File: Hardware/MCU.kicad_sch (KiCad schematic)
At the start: 40 parts, among them SW301 RESET, U301 STM32F722ZETx, Y301 24MHz

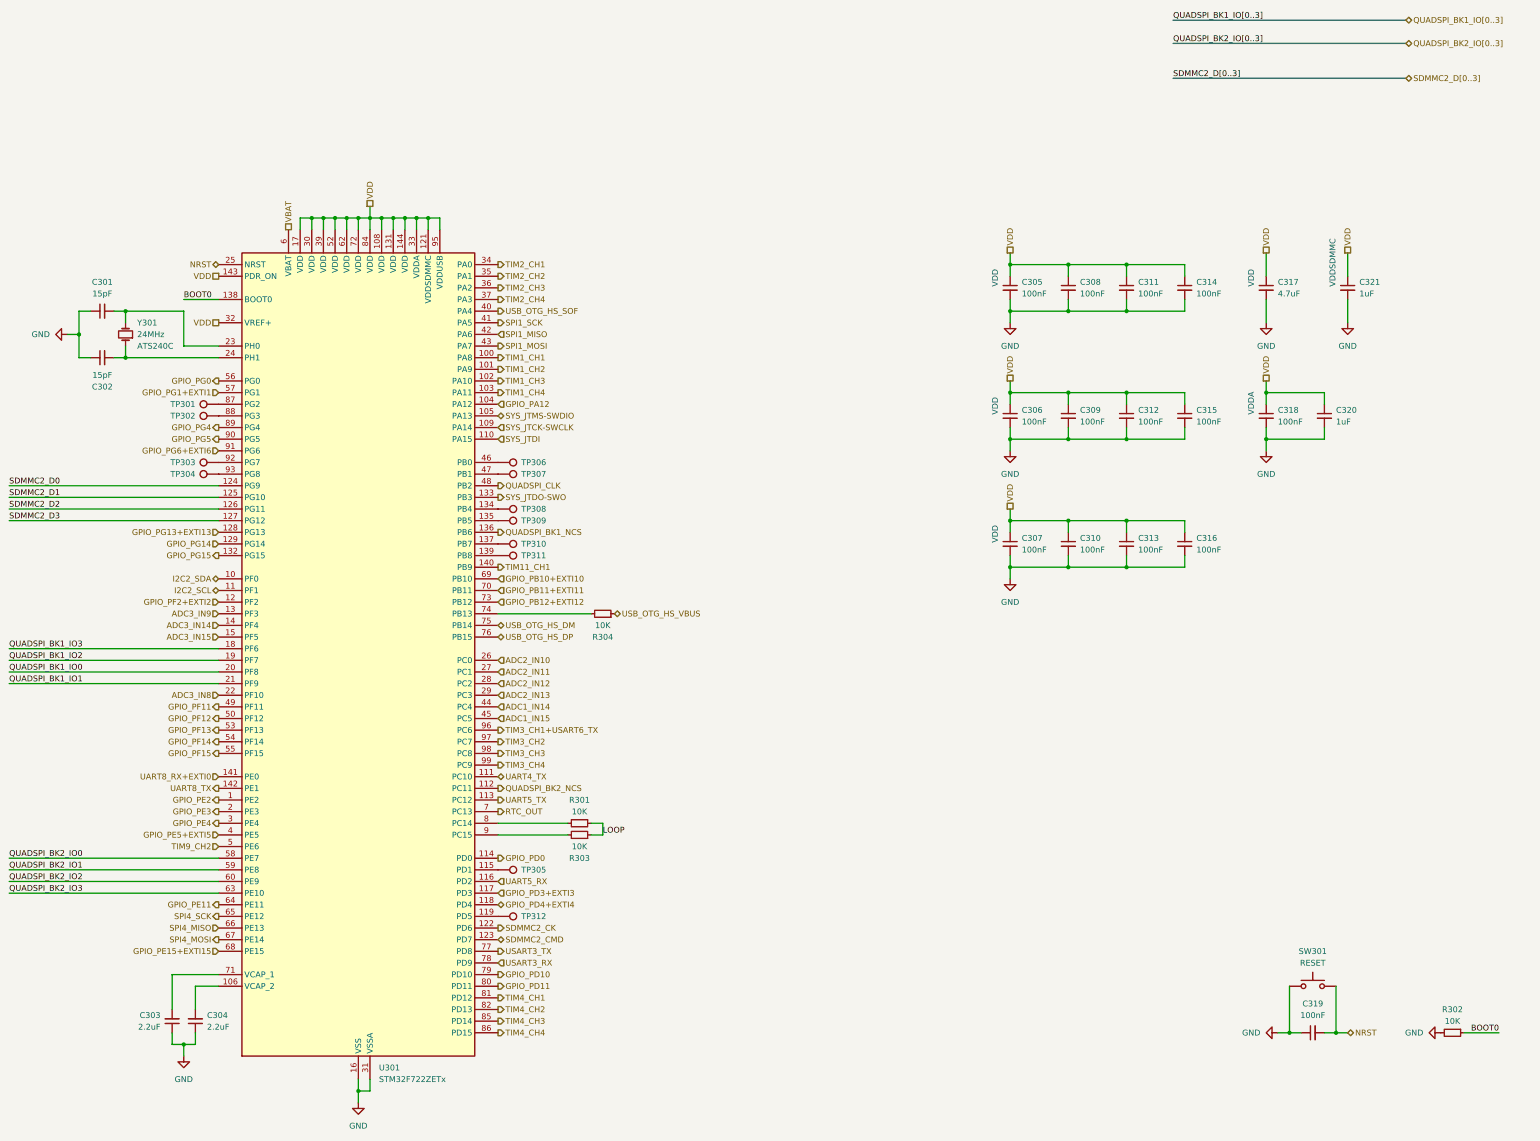
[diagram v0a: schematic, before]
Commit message: Schematic layout fixes
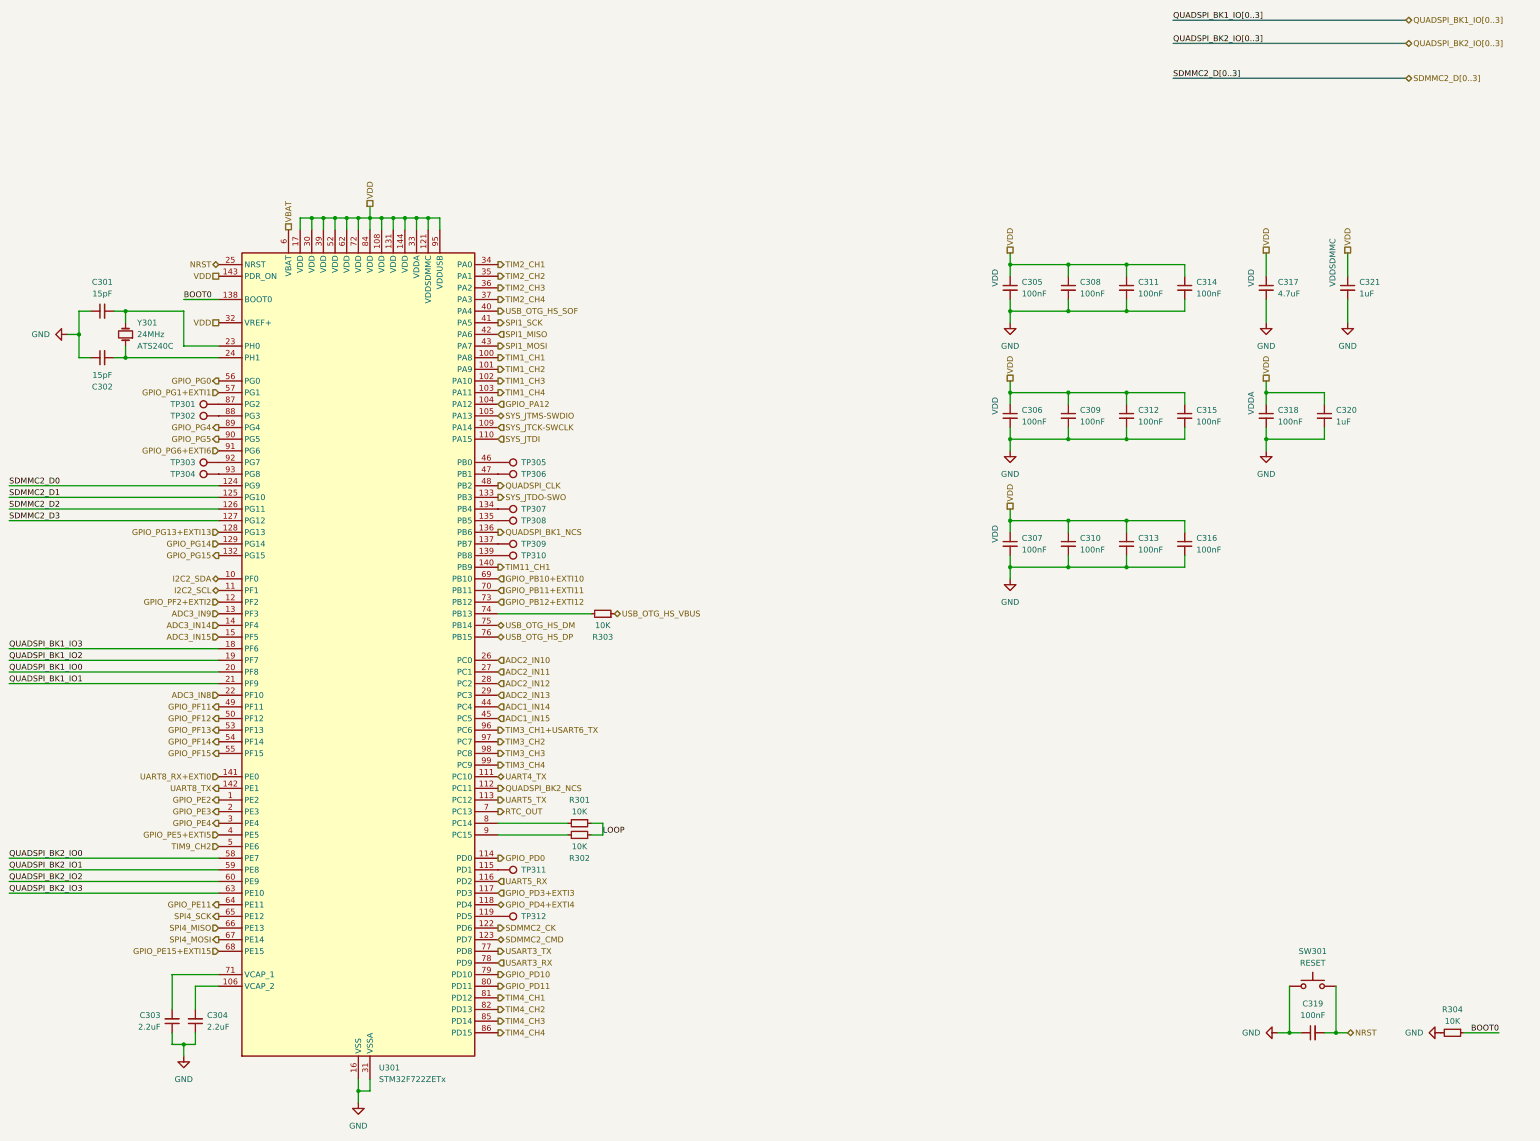
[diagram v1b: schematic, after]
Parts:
- renumbered R303 to R302, R304 to R303, R302 to R304, TP306 to TP305, TP307 to TP306, TP308 to TP307, TP309 to TP308, TP310 to TP309, TP311 to TP310, TP305 to TP311
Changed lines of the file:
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@@
   (symbol (lib_id "Connector:TestPoint") (at 182.88 142.24 270) (unit 1)
     (in_bom yes) (on_board yes) (dnp no) (fields_autoplaced)
-    (property "Reference" "TP311" (at 187.96 142.24 90)
+    (property "Reference" "TP310" (at 187.96 142.24 90)
       (effects (font (size 1.27 1.27)) (justify left))
     )
@@
       (project "Avionus_Flight_Controller"
         (path "/ddc7e940-0588-4587-8902-8ced9e615ace/fb82246b-9ed4-401c-b8a1-7e9ae6260bc5"
-          (reference "TP311") (unit 1)
+          (reference "TP310") (unit 1)
         )
       )
@@
   (symbol (lib_id "Connector:TestPoint") (at 182.88 124.46 270) (unit 1)
     (in_bom yes) (on_board yes) (dnp no) (fields_autoplaced)
-    (property "Reference" "TP307" (at 187.96 124.46 90)
+    (property "Reference" "TP306" (at 187.96 124.46 90)
       (effects (font (size 1.27 1.27)) (justify left))
     )
@@
       (project "Avionus_Flight_Controller"
         (path "/ddc7e940-0588-4587-8902-8ced9e615ace/fb82246b-9ed4-401c-b8a1-7e9ae6260bc5"
+          (reference "TP306") (unit 1)
+        )
+      )
+    )
+  )
+  (symbol (lib_id "Connector:TestPoint") (at 182.88 139.7 270) (unit 1)
+    (in_bom yes) (on_board yes) (dnp no) (fields_autoplaced)
+    (property "Reference" "TP309" (at 187.96 139.7 90)
+      (effects (font (size 1.27 1.27)) (justify left))
+    )
+    (property "Value" "~" (at 187.96 140.97 90)
+      (effects (font (size 1.27 1.27)) (justify left))
+    )
+    (property "Footprint" "TestPoint:TestPoint_Pad_D1.0mm" (at 182.88 144.78 0)
+      (effects (font (size 1.27 1.27)) hide)
+    )
+    (property "Datasheet" "~" (at 182.88 144.78 0)
+      (effects (font (size 1.27 1.27)) hide)
+    )
+    (pin "1")
+    (instances
+      (project "Avionus_Flight_Controller"
+        (path "/ddc7e940-0588-4587-8902-8ced9e615ace/fb82246b-9ed4-401c-b8a1-7e9ae6260bc5"
+          (reference "TP309") (unit 1)
+        )
+      )
+    )
+  )
+  (symbol (lib_id "Connector:TestPoint") (at 182.88 220.98 270) (unit 1)
+    (in_bom yes) (on_board yes) (dnp no) (fields_autoplaced)
+    (property "Reference" "TP312" (at 187.96 220.98 90)
+      (effects (font (size 1.27 1.27)) (justify left))
+    )
+    (property "Value" "~" (at 187.96 222.25 90)
+      (effects (font (size 1.27 1.27)) (justify left))
+    )
+    (property "Footprint" "TestPoint:TestPoint_Pad_D1.0mm" (at 182.88 226.06 0)
+      (effects (font (size 1.27 1.27)) hide)
+    )
+    (property "Datasheet" "~" (at 182.88 226.06 0)
+      (effects (font (size 1.27 1.27)) hide)
+    )
+    (pin "1")
+    (instances
+      (project "Avionus_Flight_Controller"
+        (path "/ddc7e940-0588-4587-8902-8ced9e615ace/fb82246b-9ed4-401c-b8a1-7e9ae6260bc5"
+          (reference "TP312") (unit 1)
+        )
+      )
+    )
+  )
+  (symbol (lib_id "Connector:TestPoint") (at 182.88 132.08 270) (unit 1)
+    (in_bom yes) (on_board yes) (dnp no) (fields_autoplaced)
+    (property "Reference" "TP307" (at 187.96 132.08 90)
+      (effects (font (size 1.27 1.27)) (justify left))
+    )
+    (property "Value" "~" (at 187.96 133.35 90)
+      (effects (font (size 1.27 1.27)) (justify left))
+    )
+    (property "Footprint" "TestPoint:TestPoint_Pad_D1.0mm" (at 182.88 137.16 0)
+      (effects (font (size 1.27 1.27)) hide)
+    )
+    (property "Datasheet" "~" (at 182.88 137.16 0)
+      (effects (font (size 1.27 1.27)) hide)
+    )
+    (pin "1")
+    (instances
+      (project "Avionus_Flight_Controller"
+        (path "/ddc7e940-0588-4587-8902-8ced9e615ace/fb82246b-9ed4-401c-b8a1-7e9ae6260bc5"
           (reference "TP307") (unit 1)
-        )
-      )
-    )
-  )
-  (symbol (lib_id "Connector:TestPoint") (at 182.88 139.7 270) (unit 1)
-    (in_bom yes) (on_board yes) (dnp no) (fields_autoplaced)
-    (property "Reference" "TP310" (at 187.96 139.7 90)
-      (effects (font (size 1.27 1.27)) (justify left))
-    )
-    (property "Value" "~" (at 187.96 140.97 90)
-      (effects (font (size 1.27 1.27)) (justify left))
-    )
-    (property "Footprint" "TestPoint:TestPoint_Pad_D1.0mm" (at 182.88 144.78 0)
-      (effects (font (size 1.27 1.27)) hide)
-    )
-    (property "Datasheet" "~" (at 182.88 144.78 0)
-      (effects (font (size 1.27 1.27)) hide)
-    )
-    (pin "1")
-    (instances
-      (project "Avionus_Flight_Controller"
-        (path "/ddc7e940-0588-4587-8902-8ced9e615ace/fb82246b-9ed4-401c-b8a1-7e9ae6260bc5"
-          (reference "TP310") (unit 1)
-        )
-      )
-    )
-  )
-  (symbol (lib_id "Connector:TestPoint") (at 182.88 220.98 270) (unit 1)
-    (in_bom yes) (on_board yes) (dnp no) (fields_autoplaced)
-    (property "Reference" "TP312" (at 187.96 220.98 90)
-      (effects (font (size 1.27 1.27)) (justify left))
-    )
-    (property "Value" "~" (at 187.96 222.25 90)
-      (effects (font (size 1.27 1.27)) (justify left))
-    )
-    (property "Footprint" "TestPoint:TestPoint_Pad_D1.0mm" (at 182.88 226.06 0)
-      (effects (font (size 1.27 1.27)) hide)
-    )
-    (property "Datasheet" "~" (at 182.88 226.06 0)
-      (effects (font (size 1.27 1.27)) hide)
-    )
-    (pin "1")
-    (instances
-      (project "Avionus_Flight_Controller"
-        (path "/ddc7e940-0588-4587-8902-8ced9e615ace/fb82246b-9ed4-401c-b8a1-7e9ae6260bc5"
-          (reference "TP312") (unit 1)
-        )
-      )
-    )
-  )
-  (symbol (lib_id "Connector:TestPoint") (at 182.88 132.08 270) (unit 1)
-    (in_bom yes) (on_board yes) (dnp no) (fields_autoplaced)
-    (property "Reference" "TP308" (at 187.96 132.08 90)
-      (effects (font (size 1.27 1.27)) (justify left))
-    )
-    (property "Value" "~" (at 187.96 133.35 90)
-      (effects (font (size 1.27 1.27)) (justify left))
-    )
-    (property "Footprint" "TestPoint:TestPoint_Pad_D1.0mm" (at 182.88 137.16 0)
-      (effects (font (size 1.27 1.27)) hide)
-    )
-    (property "Datasheet" "~" (at 182.88 137.16 0)
-      (effects (font (size 1.27 1.27)) hide)
-    )
-    (pin "1")
-    (instances
-      (project "Avionus_Flight_Controller"
-        (path "/ddc7e940-0588-4587-8902-8ced9e615ace/fb82246b-9ed4-401c-b8a1-7e9ae6260bc5"
-          (reference "TP308") (unit 1)
         )
       )
@@
   (symbol (lib_id "Connector:TestPoint") (at 182.88 134.62 270) (unit 1)
     (in_bom yes) (on_board yes) (dnp no) (fields_autoplaced)
-    (property "Reference" "TP309" (at 187.96 134.62 90)
+    (property "Reference" "TP308" (at 187.96 134.62 90)
       (effects (font (size 1.27 1.27)) (justify left))
     )
@@
       (project "Avionus_Flight_Controller"
         (path "/ddc7e940-0588-4587-8902-8ced9e615ace/fb82246b-9ed4-401c-b8a1-7e9ae6260bc5"
-          (reference "TP309") (unit 1)
+          (reference "TP308") (unit 1)
         )
       )
@@
   (symbol (lib_id "Device:R_Small") (at 205.74 154.94 270) (mirror x) (unit 1)
     (in_bom yes) (on_board yes) (dnp no)
-    (property "Reference" "R304" (at 205.74 160.02 90)
+    (property "Reference" "R303" (at 205.74 160.02 90)
       (effects (font (size 1.27 1.27)))
     )
@@
       (project "Avionus_Flight_Controller"
         (path "/ddc7e940-0588-4587-8902-8ced9e615ace/fb82246b-9ed4-401c-b8a1-7e9ae6260bc5"
-          (reference "R304") (unit 1)
+          (reference "R303") (unit 1)
         )
       )
@@
   (symbol (lib_id "Device:R_Small") (at 200.66 203.2 270) (mirror x) (unit 1)
     (in_bom yes) (on_board yes) (dnp no)
-    (property "Reference" "R303" (at 200.66 208.28 90)
+    (property "Reference" "R302" (at 200.66 208.28 90)
       (effects (font (size 1.27 1.27)))
     )
@@
       (project "Avionus_Flight_Controller"
         (path "/ddc7e940-0588-4587-8902-8ced9e615ace/fb82246b-9ed4-401c-b8a1-7e9ae6260bc5"
-          (reference "R303") (unit 1)
+          (reference "R302") (unit 1)
         )
       )
@@
   (symbol (lib_id "Connector:TestPoint") (at 182.88 121.92 270) (unit 1)
     (in_bom yes) (on_board yes) (dnp no) (fields_autoplaced)
-    (property "Reference" "TP306" (at 187.96 121.92 90)
+    (property "Reference" "TP305" (at 187.96 121.92 90)
       (effects (font (size 1.27 1.27)) (justify left))
     )
@@
       (project "Avionus_Flight_Controller"
         (path "/ddc7e940-0588-4587-8902-8ced9e615ace/fb82246b-9ed4-401c-b8a1-7e9ae6260bc5"
-          (reference "TP306") (unit 1)
+          (reference "TP305") (unit 1)
         )
       )
@@
   (symbol (lib_id "Connector:TestPoint") (at 182.88 210.82 270) (unit 1)
     (in_bom yes) (on_board yes) (dnp no) (fields_autoplaced)
-    (property "Reference" "TP305" (at 187.96 210.82 90)
+    (property "Reference" "TP311" (at 187.96 210.82 90)
       (effects (font (size 1.27 1.27)) (justify left))
     )
@@
       (project "Avionus_Flight_Controller"
         (path "/ddc7e940-0588-4587-8902-8ced9e615ace/fb82246b-9ed4-401c-b8a1-7e9ae6260bc5"
-          (reference "TP305") (unit 1)
+          (reference "TP311") (unit 1)
         )
       )
@@
   (symbol (lib_id "Device:R_Small") (at 391.16 246.38 270) (unit 1)
     (in_bom yes) (on_board yes) (dnp no) (fields_autoplaced)
-    (property "Reference" "R302" (at 391.16 241.3 90)
+    (property "Reference" "R304" (at 391.16 241.3 90)
       (effects (font (size 1.27 1.27)))
     )
@@
       (project "Avionus_Flight_Controller"
         (path "/ddc7e940-0588-4587-8902-8ced9e615ace/fb82246b-9ed4-401c-b8a1-7e9ae6260bc5"
-          (reference "R302") (unit 1)
-        )
-      )
+          (reference "R304") (unit 1)
+        )
+      )

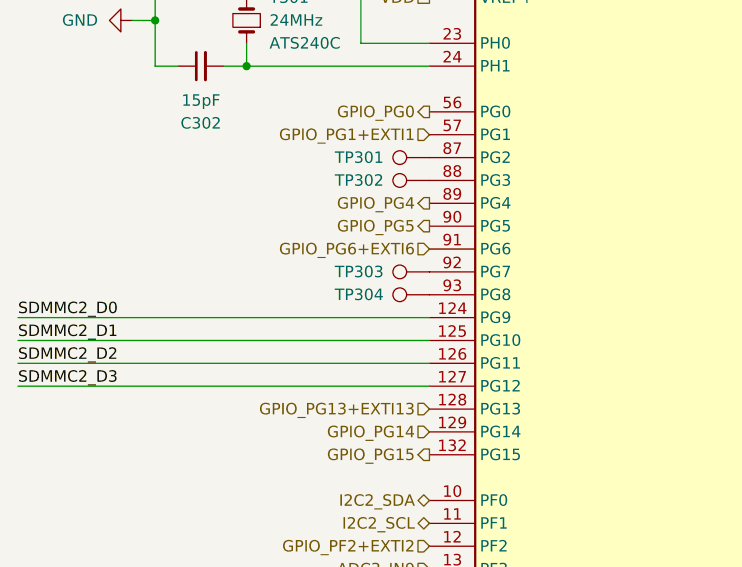
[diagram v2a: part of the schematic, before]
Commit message: Add lidar2
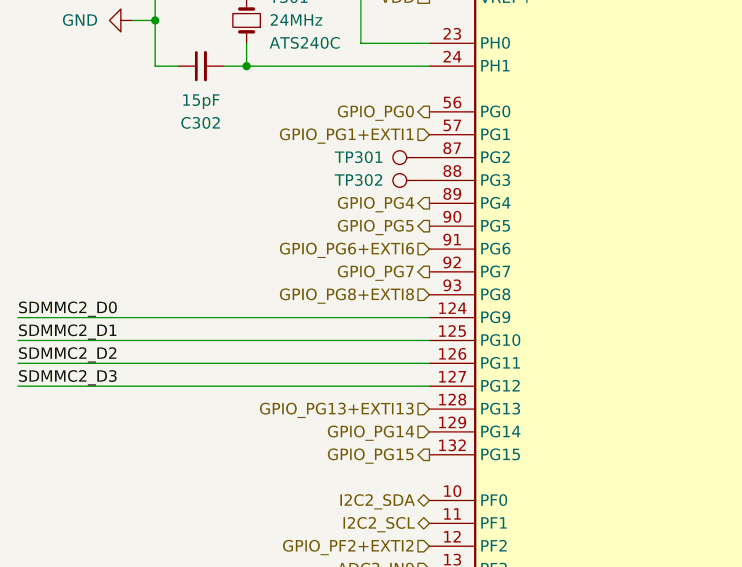
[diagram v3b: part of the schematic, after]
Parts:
- removed TP303, TP304: ~, TestPoint:TestPoint_Pad_D1.0mm, symbol Connector:TestPoint
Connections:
- net GPIO_PG8+EXTI8: now reaches U301.93 (PG8)
- net GPIO_PG7: now reaches U301.92 (PG7)
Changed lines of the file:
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@@
     (effects (font (size 1.27 1.27)) (justify left))
+  )
+  (hierarchical_label "GPIO_PG7" (shape output) (at 121.92 121.92 180) (fields_autoplaced)
+    (effects (font (size 1.27 1.27)) (justify right))
   )
   (hierarchical_label "VDD" (shape passive) (at 121.92 91.44 180) (fields_autoplaced)
@@
   (hierarchical_label "ADC2_IN12" (shape input) (at 182.88 170.18 0) (fields_autoplaced)
     (effects (font (size 1.27 1.27)) (justify left))
+  )
+  (hierarchical_label "GPIO_PG8+EXTI8" (shape input) (at 121.92 124.46 180) (fields_autoplaced)
+    (effects (font (size 1.27 1.27)) (justify right))
   )
   (hierarchical_label "TIM4_CH2" (shape output) (at 182.88 241.3 0) (fields_autoplaced)
@@
         (path "/ddc7e940-0588-4587-8902-8ced9e615ace/fb82246b-9ed4-401c-b8a1-7e9ae6260bc5"
           (reference "C312") (unit 1)
-        )
-      )
-    )
-  )
-  (symbol (lib_id "Connector:TestPoint") (at 121.92 124.46 90) (unit 1)
-    (in_bom yes) (on_board yes) (dnp no) (fields_autoplaced)
-    (property "Reference" "TP304" (at 116.84 124.46 90)
-      (effects (font (size 1.27 1.27)) (justify left))
-    )
-    (property "Value" "~" (at 116.84 123.19 90)
-      (effects (font (size 1.27 1.27)) (justify left))
-    )
-    (property "Footprint" "TestPoint:TestPoint_Pad_D1.0mm" (at 121.92 119.38 0)
-      (effects (font (size 1.27 1.27)) hide)
-    )
-    (property "Datasheet" "~" (at 121.92 119.38 0)
-      (effects (font (size 1.27 1.27)) hide)
-    )
-    (pin "1")
-    (instances
-      (project "Avionus_Flight_Controller"
-        (path "/ddc7e940-0588-4587-8902-8ced9e615ace/fb82246b-9ed4-401c-b8a1-7e9ae6260bc5"
-          (reference "TP304") (unit 1)
         )
       )
@@
         )
       )
-    )
-  )
-  (symbol (lib_id "Connector:TestPoint") (at 121.92 121.92 90) (unit 1)
-    (in_bom yes) (on_board yes) (dnp no) (fields_autoplaced)
-    (property "Reference" "TP303" (at 116.84 121.92 90)
-      (effects (font (size 1.27 1.27)) (justify left))
-    )
-    (property "Value" "~" (at 116.84 120.65 90)
-      (effects (font (size 1.27 1.27)) (justify left))
-    )
-    (property "Footprint" "TestPoint:TestPoint_Pad_D1.0mm" (at 121.92 116.84 0)
-      (effects (font (size 1.27 1.27)) hide)
-    )
-    (property "Datasheet" "~" (at 121.92 116.84 0)
-      (effects (font (size 1.27 1.27)) hide)
-    )
-    (pin "1")
-    (instances
-      (project "Avionus_Flight_Controller"
-        (path "/ddc7e940-0588-4587-8902-8ced9e615ace/fb82246b-9ed4-401c-b8a1-7e9ae6260bc5"
-          (reference "TP303") (unit 1)
-        )
-      )
